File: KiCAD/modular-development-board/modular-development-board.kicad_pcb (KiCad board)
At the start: 2 copper layers, 79 x 79 mm, 64 parts, among them J1 Power In, J10 DHT11-LEDS, J11 Buzzzer-Light, J12 USB_B_Micro, J13 UART, J2 5V Out, J3 3V3 Out, J4 GND, J5 Digital 1, J6 Digital 2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

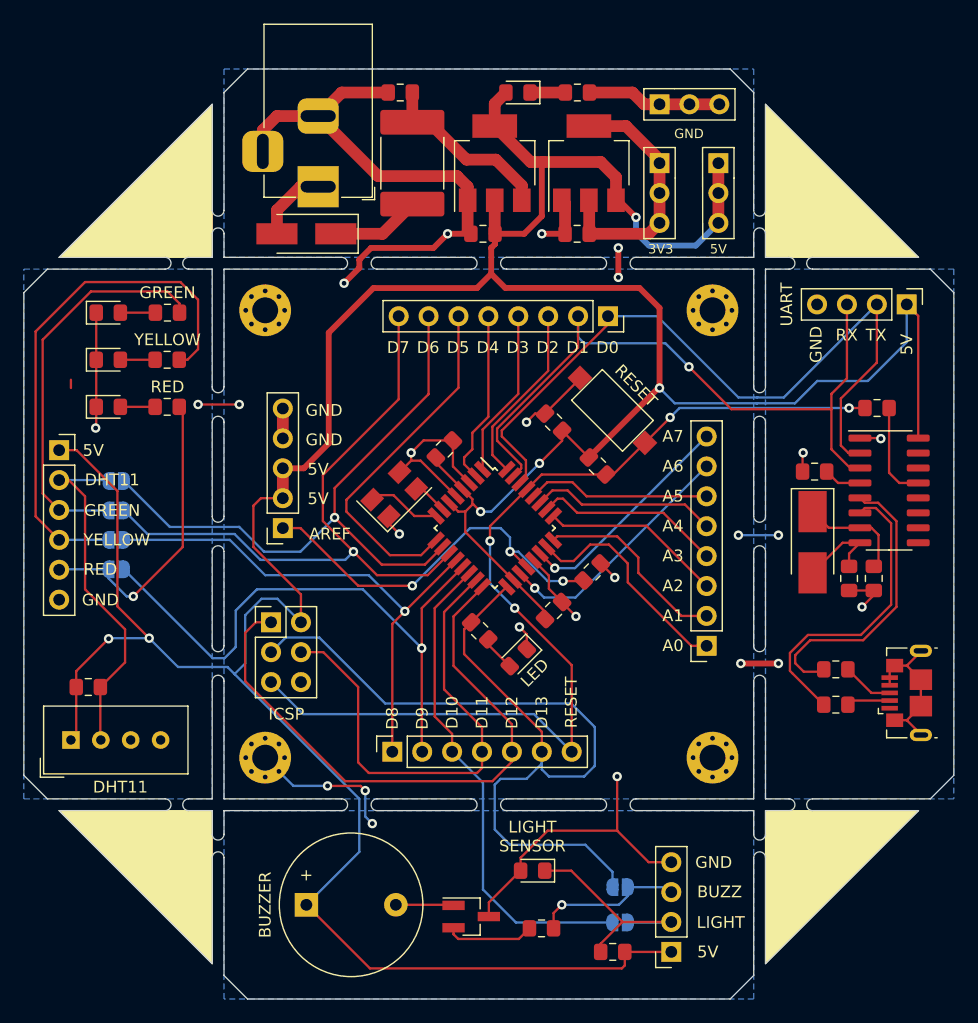
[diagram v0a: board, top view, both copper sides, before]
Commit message: Added modular developmend board design and test software.
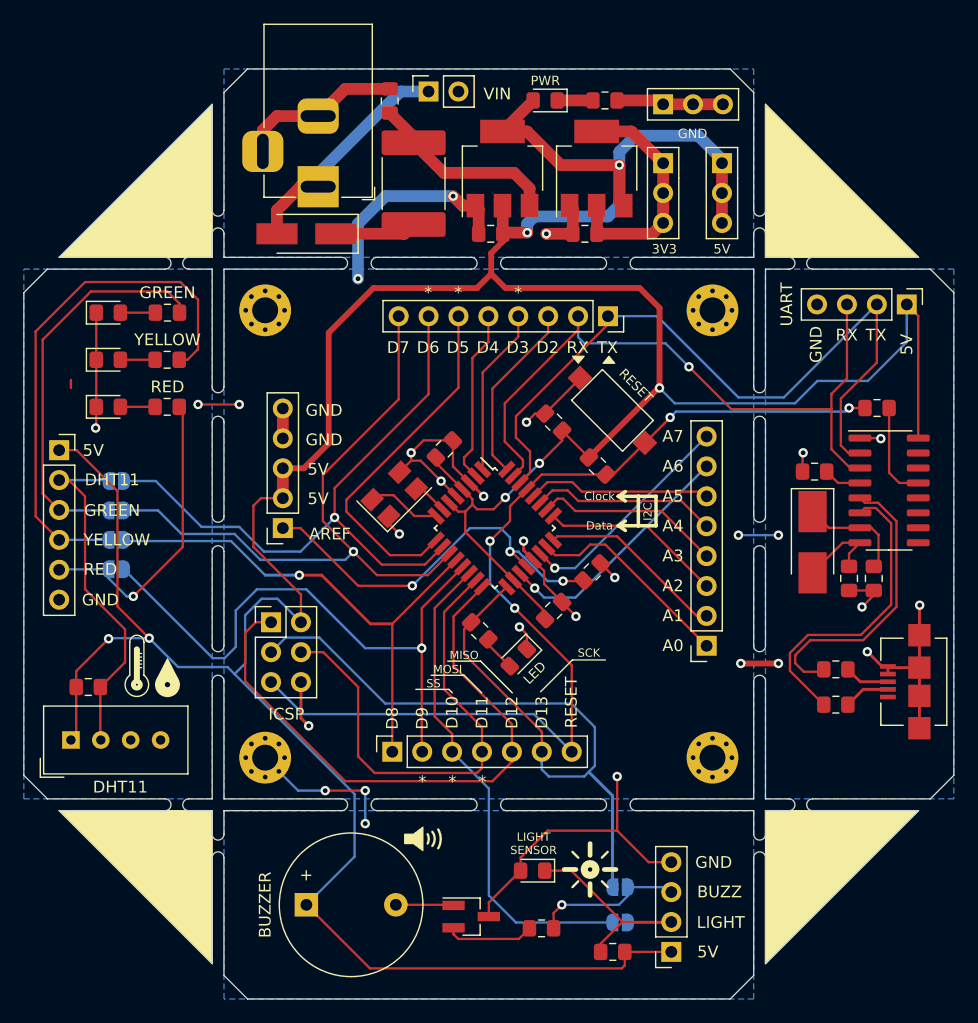
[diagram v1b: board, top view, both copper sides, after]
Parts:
- removed REF**: KiCad-Logo2_5mm_SilkScreen, Symbol:KiCad-Logo2_5mm_SilkScreen
- added J14: Power In, Connector_PinSocket_2.54mm:PinSocket_1x02_P2.54mm_Vertical, F.Cu at (65.4, 38.9)
- F1: value 2A 24V PTC -> FSMD200-242920-R
- J12: footprint Connector_USB:USB_Micro-B_GCT_USB3076-30-A -> Footprints:KLS1-233-Micro-USB
- moved R3 2.44 mm to (80.4, 39.7)
- moved D3 2.41 mm to (75.3, 39.7)
- moved J12 1.86 mm to (104.4, 89.0)
- moved F1 1.74 mm to (64.1, 46.7)
- moved C5 1.15 mm to (62.1, 39.7), turned to 90 degrees
- moved U2 0.80 mm to (71.7, 45.5)
- moved U3 0.80 mm to (79.7, 45.5)
- moved C6 0.66 mm to (70.7, 51.0)
- moved C7 0.66 mm to (78.7, 51.0)
- moved J2 0.30 mm to (90.3, 45.0)
- moved J3 0.30 mm to (85.3, 45.0)
- moved J4 0.30 mm to (85.3, 40.0)
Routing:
- net Net-(D1-Pad2): track 6.83 -> 20.2 mm
- net /D13: track 81.7 -> 70.9 mm
- net GND: track 179.7 -> 171.6 mm, vias 25 -> 29
- net +5V: track 314.2 -> 319.8 mm, vias 6 -> 7
- net +3V3: track 21.8 -> 20.2 mm
- net /A0: track 19.2 -> 17.8 mm
- net VCC: track 15.3 -> 16.3 mm
- net /A1: track 16.7 -> 15.9 mm
- net Net-(J12-Pad2): track 3.69 -> 4.43 mm
- net /D0: track 63.0 -> 62.3 mm
- net /D8: track 44.9 -> 44.3 mm
- net Net-(D1-Pad1): track 7.55 -> 6.94 mm
- net Net-(J12-Pad3): track 4.38 -> 3.83 mm
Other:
- board text added: "*"
- board text added: "Clock"
- board text added: "Data"
- board text added: "I2C"
- board text added: "Input Voltage: 7V<VIN<16V Output Current: Max. 1A"
- board text added: "MISO"
- board text added: "MOSI"
- board text added: "PWR"
- board text added: "SCK"
- board text added: "SS"
- board text added: "VIN"
- board text removed: "D0"
- board text removed: "D1"
